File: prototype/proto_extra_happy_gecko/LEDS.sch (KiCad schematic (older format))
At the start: 76 parts

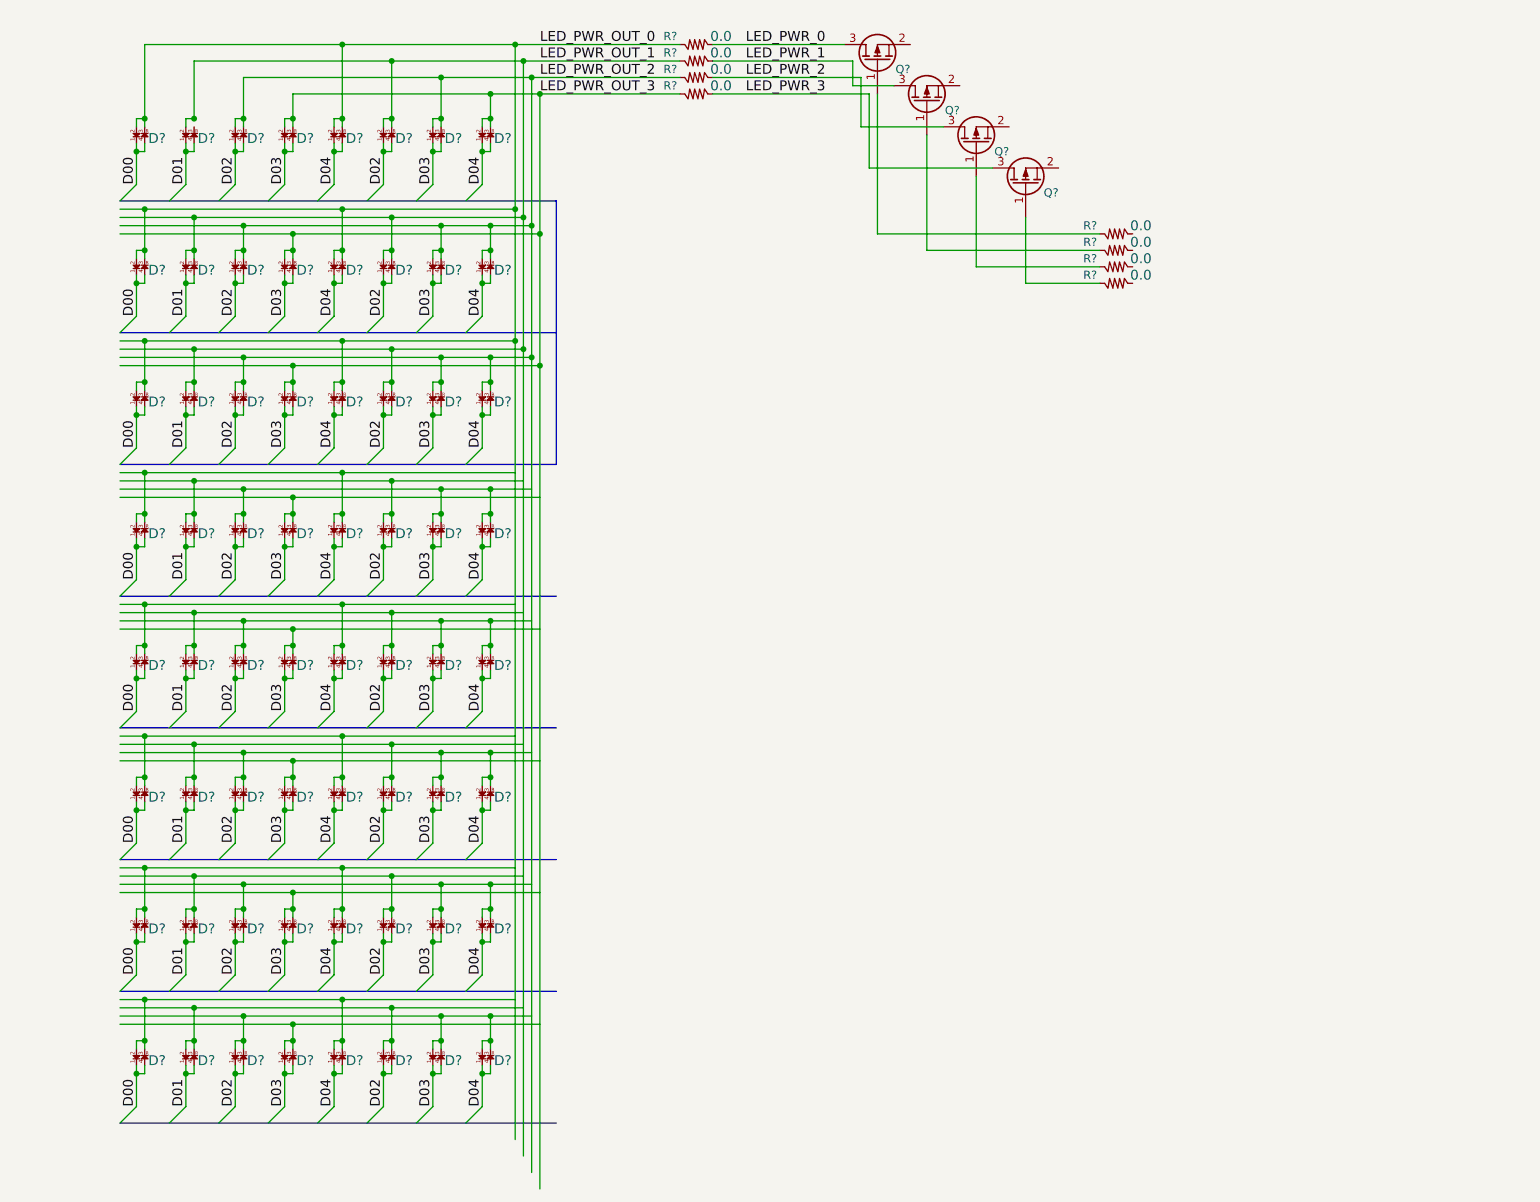
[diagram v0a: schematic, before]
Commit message: Added all leds, 3.3Vreg, and routed busses
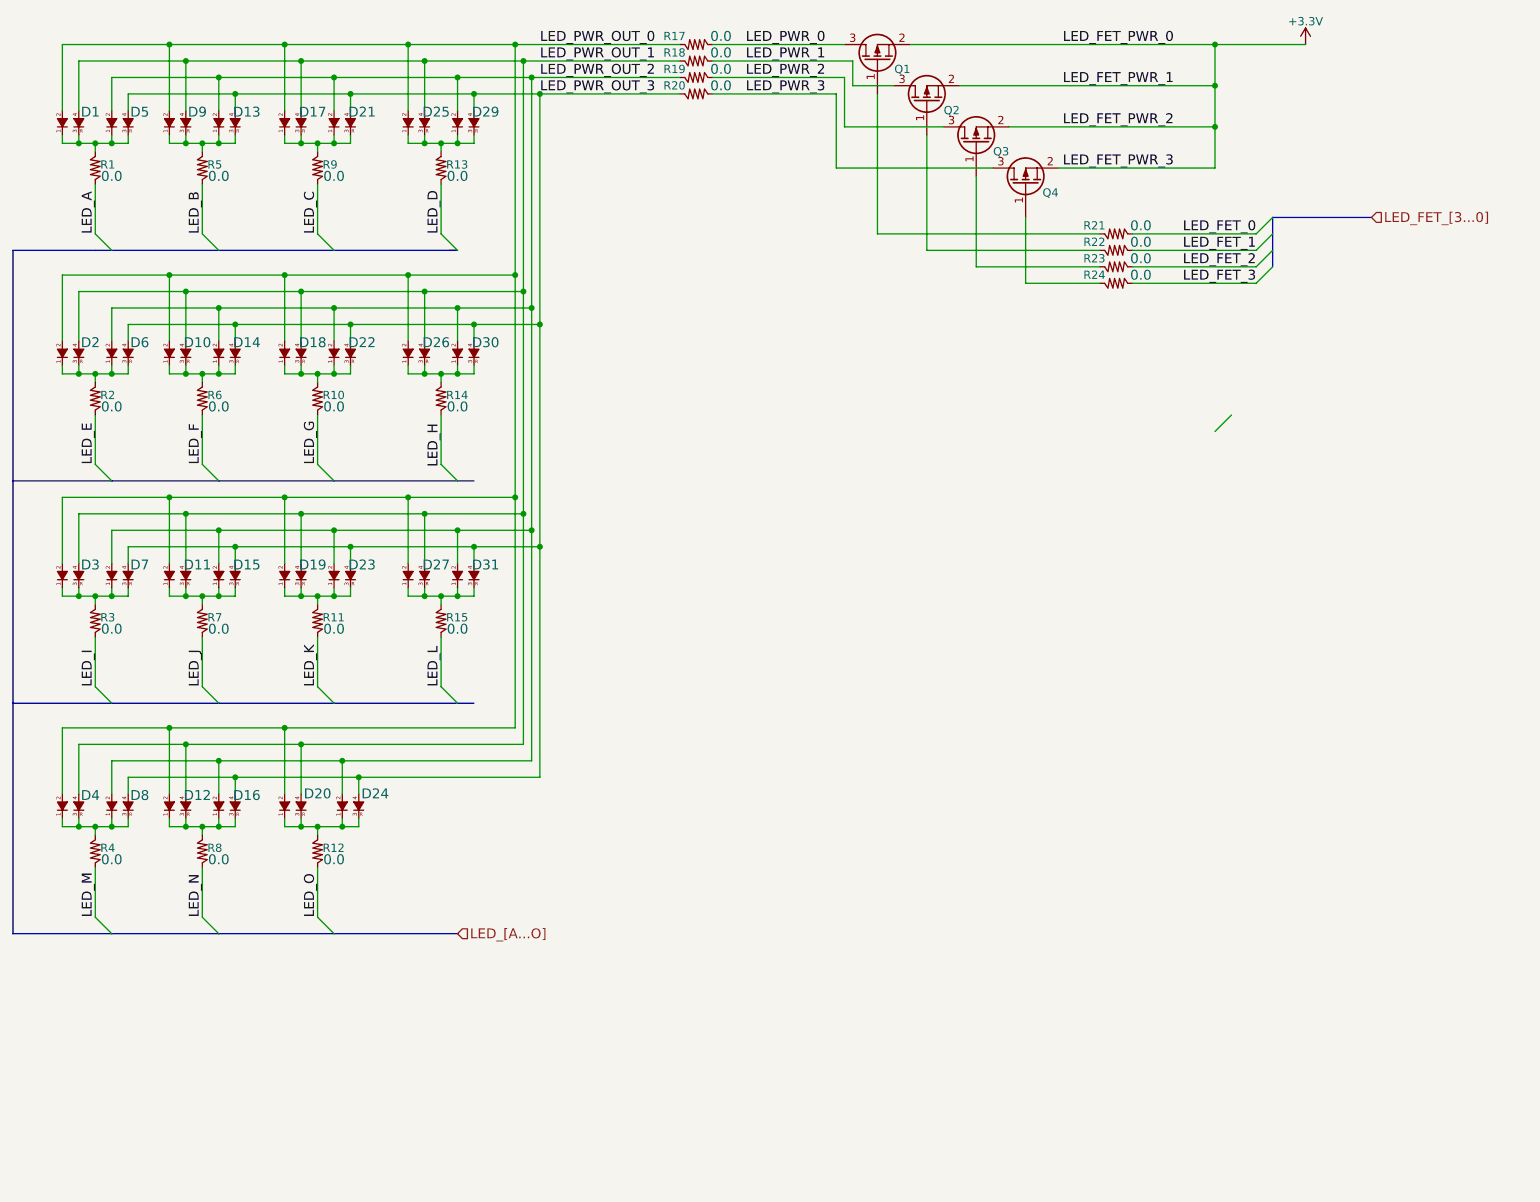
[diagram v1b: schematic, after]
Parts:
- removed D? (x64): LED_RED/BLUE, symbol LED_RED/BLUE
- added D1, D10, D11, D12, D13, D14, D15, D16, D17, D18, D19, D2, D20, D21, D22, D23, D24, D25, D26, D27, D29, D3, D30, D31, D4, D5, D6, D7, D8, D9: LED_RED/BLUE_ALT, symbol LED_RED/BLUE_ALT
- added R1, R10, R11, R12, R13, R14, R15, R2, R3, R4, R5, R6, R7, R8, R9: RES_0R0_0402, symbol RES_0R0_0402
- gave numbers to parts that had none: 12
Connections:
- net labels added: +3.3V, LED_A, LED_B, LED_C, LED_D, LED_E, LED_F, LED_FET_0, LED_FET_1, LED_FET_2, LED_FET_3, LED_FET_PWR_0, LED_FET_PWR_1, LED_FET_PWR_2, LED_FET_PWR_3, LED_FET_[3...0], LED_G, LED_H, LED_I, LED_J, LED_K, LED_L, LED_M, LED_N, LED_O, LED_[A...O]
- net labels removed: D00, D01, D02, D03, D04
- wire segments 438 -> 316
